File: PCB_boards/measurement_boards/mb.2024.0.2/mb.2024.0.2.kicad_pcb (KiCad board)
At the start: 2 copper layers, 247.8 x 124.2 mm, 121 parts, among them J1 DSP_out_12v_GND, J10 DSP+, J11 Screw_Terminal_VMN, J12 Conn_01x08_Female, J13 Connector_I2C_for_mux, J14 Conn_01x02_Female, J15 Conn_01x08_Female, J16 RX_bat, J17 DSP GND, J18 ELEC_M, J19 ELEC_N, J2 DPS5005_input_0_to_50V, J20 shunt +, J21 shunt -, J22 Conn_01x04_Female, J23 Conn_01x05_Female, J24 Connector_I2C_for_MC, J25 Conn_01x04_Female, J26 Conn_01x05_Female, J3 Screw_Terminal_AB, J4 Conn_01x08_Female, J5 Conn_01x04_Female, J6 Conn_01x08_Female, J7 Raspberry_Pi_2_3, J8 Connector_I2C_for_MCP23008, J9 TX_bat, K1 G5LE-1, K2 G5LE-1, K3 G5LE-1, K4 G5LE-1, K5 G5LE-1, K6 G5LE-1, Q1 ZVN4206ASTZ, Q2 ZVN4206ASTZ, Q3 ZVN4206ASTZ, Q4 ZVN4206ASTZ, Q5 ZVN4206ASTZ, Q6 ZVN4206ASTZ, U1 MCP23008-xP, U10 DG411xJ, U2 OP07, U3 24LC02, U4 1085, U5 1085, U6 OP07, U7 REF03GP, U8 MCP23008-xP, U9 OP07

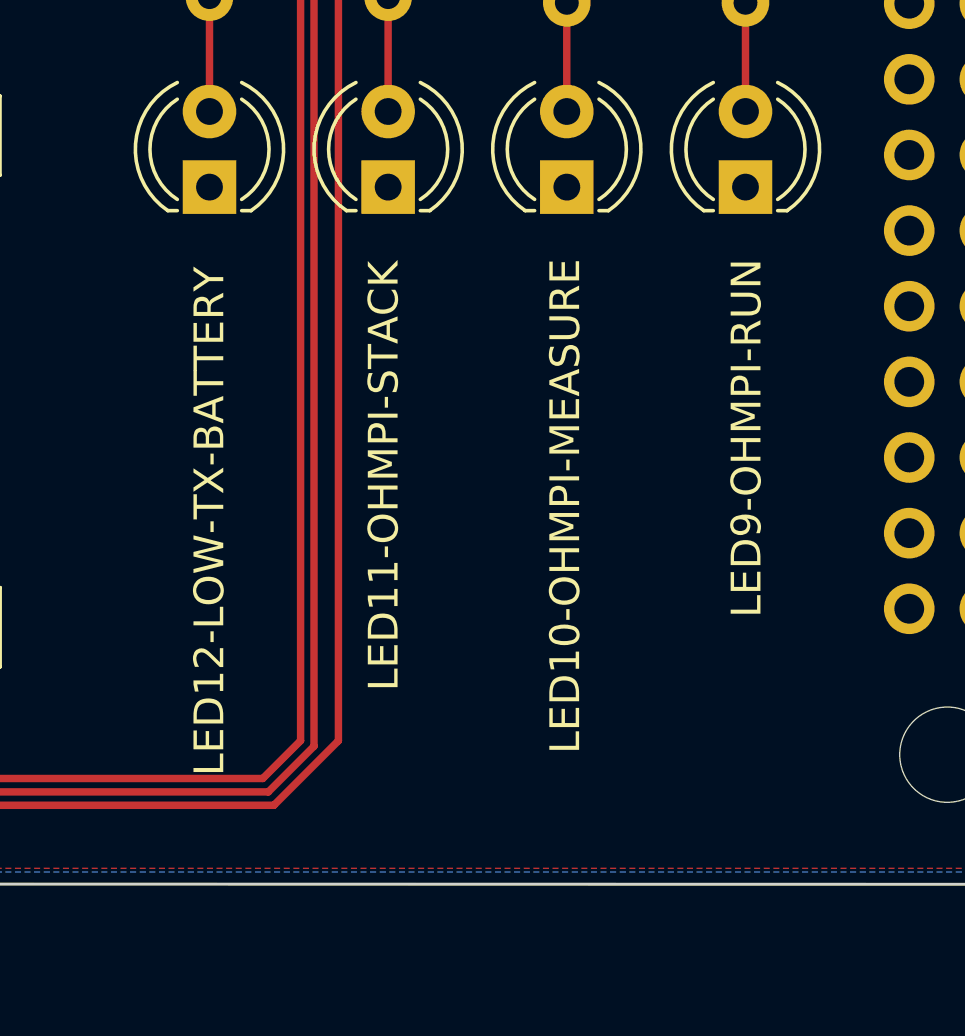
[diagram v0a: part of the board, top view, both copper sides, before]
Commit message: update diode 1n4007
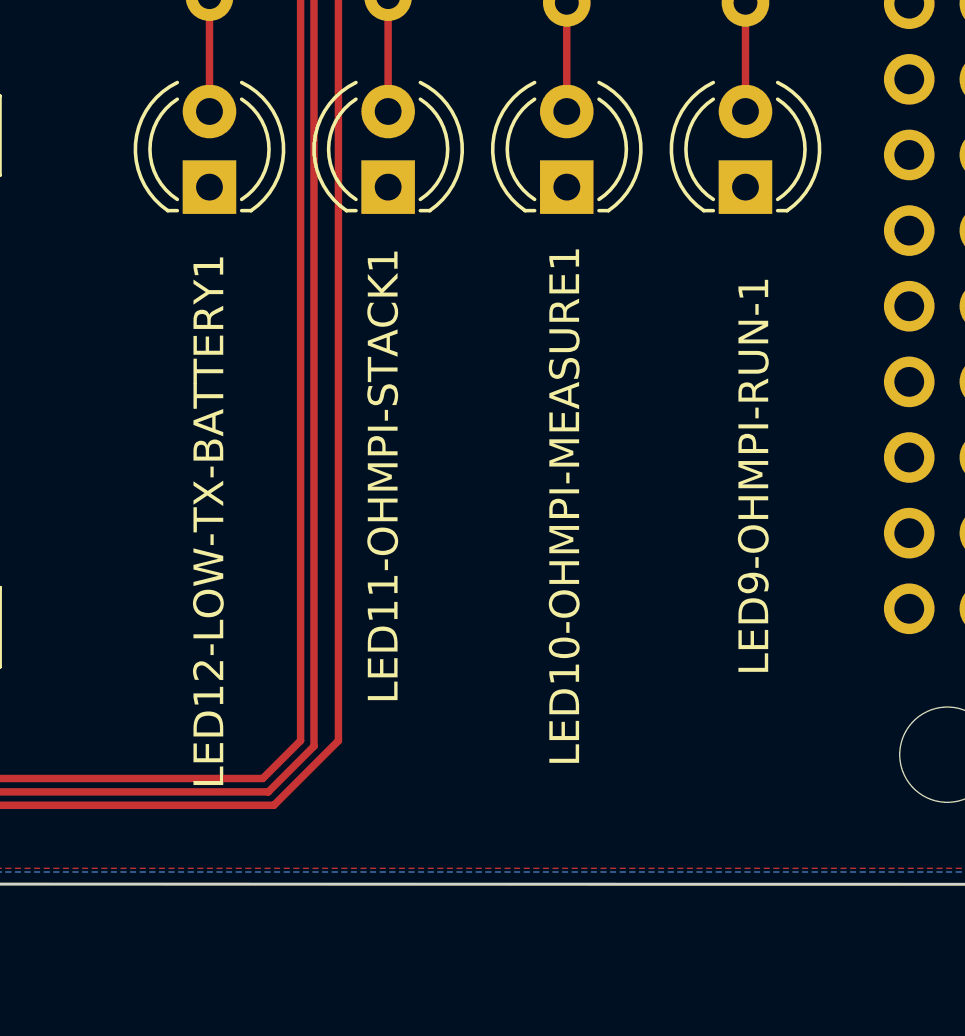
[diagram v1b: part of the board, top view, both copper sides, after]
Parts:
- D1, D10, D11, D12, D2, D9: value 1N4001 -> 1N4007
- renumbered LED10-OHMPI-MEASURE to LED10-OHMPI-MEASURE1, LED11-OHMPI-STACK to LED11-OHMPI-STACK1, LED12-LOW-TX-BATTERY to LED12-LOW-TX-BATTERY1, LED9-OHMPI-RUN to LED9-OHMPI-RUN-1
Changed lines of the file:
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@@
     (property "ki_keywords" "LED diode")
     (attr through_hole)
-    (fp_text reference "LED10-OHMPI-MEASURE" (at -10.716 -0.05 90) (layer "F.SilkS")
+    (fp_text reference "LED10-OHMPI-MEASURE1" (at -10.716 -0.05 90) (layer "F.SilkS")
         (effects (font (size 1 1) (thickness 0.15)))
     )
@@
         (effects (font (size 1 1) (thickness 0.15)))
     )
-    (fp_text value "1N4001" (at 10.16 2.47) (layer "F.Fab")
+    (fp_text value "1N4007" (at 10.16 2.47) (layer "F.Fab")
         (effects (font (size 1 1) (thickness 0.15)))
     )
@@
     (property "ki_keywords" "LED diode")
     (attr through_hole)
-    (fp_text reference "LED9-OHMPI-RUN" (at -8.43 0.04 90) (layer "F.SilkS")
+    (fp_text reference "LED9-OHMPI-RUN-1" (at -9.7 0.3 90) (layer "F.SilkS")
         (effects (font (size 1 1) (thickness 0.15)))
     )
@@
         (effects (font (size 1 1) (thickness 0.15)))
     )
-    (fp_text value "1N4001" (at 15.24 1.016) (layer "F.Fab")
+    (fp_text value "1N4007" (at 15.24 1.016) (layer "F.Fab")
         (effects (font (size 1 1) (thickness 0.15)))
     )
@@
         (effects (font (size 1 1) (thickness 0.15)))
     )
-    (fp_text value "1N4001" (at 5.08 2.47) (layer "F.Fab")
+    (fp_text value "1N4007" (at 5.08 2.47) (layer "F.Fab")
         (effects (font (size 1 1) (thickness 0.15)))
     )
@@
         (effects (font (size 1 1) (thickness 0.15)))
     )
-    (fp_text value "1N4001" (at 8.89 2.286) (layer "F.Fab")
+    (fp_text value "1N4007" (at 8.89 2.286) (layer "F.Fab")
         (effects (font (size 1 1) (thickness 0.15)))
     )
@@
         (effects (font (size 1 1) (thickness 0.15)))
     )
-    (fp_text value "1N4001" (at 5.08 2.47) (layer "F.Fab")
+    (fp_text value "1N4007" (at 5.08 2.47) (layer "F.Fab")
         (effects (font (size 1 1) (thickness 0.15)))
     )
@@
     (property "ki_keywords" "LED diode")
     (attr through_hole)
-    (fp_text reference "LED11-OHMPI-STACK" (at -9.7 -0.146 90) (layer "F.SilkS")
+    (fp_text reference "LED11-OHMPI-STACK1" (at -9.7 -0.146 90) (layer "F.SilkS")
         (effects (font (size 1 1) (thickness 0.15)))
     )
@@
         (effects (font (size 1 1) (thickness 0.15)))
     )
-    (fp_text value "1N4001" (at 10.668 2.5485) (layer "F.Fab")
+    (fp_text value "1N4007" (at 10.668 2.5485) (layer "F.Fab")
         (effects (font (size 1 1) (thickness 0.15)))
     )
@@
     (property "ki_keywords" "LED diode")
     (attr through_hole)
-    (fp_text reference "LED12-LOW-TX-BATTERY" (at -11.224 0 90) (layer "F.SilkS")
+    (fp_text reference "LED12-LOW-TX-BATTERY1" (at -11.224 0 90) (layer "F.SilkS")
         (effects (font (size 1 1) (thickness 0.15)))
     )
@@
     (connect_pads (clearance 0.508))
     (min_thickness 0.254) (filled_areas_thickness no)
-    (fill (thermal_gap 0.508) (thermal_bridge_width 0.508))
+    (fill yes (thermal_gap 0.508) (thermal_bridge_width 0.508))
     (polygon
       (pts
